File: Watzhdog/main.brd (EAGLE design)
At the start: 100 x 80 mm, 51 parts, among them IC1 C8051F381-GM, IC3 N25Q512A, IC6 MPU-9250, SW2 PTR1TP10R, U1 MCP73831, U2 TPS61200

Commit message: Modified circuit and filename
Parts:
- removed C6: 10uF, rcl:C0402K
- removed R18: (no value), rcl:R0402
- removed R6: 1.2M, rcl:R0402
- removed R7: 220k, rcl:R0402
- removed R8: 2M, rcl:R0402
- removed SJ1: (no value), SparkFun:SJ_3_PASTE2&3
- removed SW2: PTR1TP10R, testpad:TP10R
- added C12: 10uF, CH_passive:1206
- R5: device SparkFun:0603-RES -> rcl:R0402
- U2: value TPS61200 -> TPS61201
- moved C5 335.6 mm to (62.7, 8.51), turned to 180 degrees
- moved C2 329.8 mm to (69.4, 13.9), turned to 90 degrees
- moved JP2 297.5 mm to (47.8, 72.6)
- moved R17 275.6 mm to (22.9, 62.7), turned to 270 degrees
- moved MP 273.4 mm to (21.1, 69.6)
- moved MN 269.9 mm to (23.8, 69.7)
- moved R2 268.6 mm to (71.0, 14.0), turned to 270 degrees
- moved R15 255.5 mm to (24.7, 62.8), turned to 270 degrees
- moved FET1 252.6 mm to (23.7, 66.3)
- moved R14 229.0 mm to (72.6, 38.9), turned to 90 degrees
- moved R9 222.9 mm to (50.7, 72.6), turned to 180 degrees
- moved R13 221.9 mm to (72.6, 36.5), turned to 270 degrees
- moved LED1 219.9 mm to (53.5, 72.6)
- moved R16 215.8 mm to (15.3, 8.42)
- moved S1 213.8 mm to (72.6, 33.5)
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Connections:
- removed net 3.3V: R6.1, SJ1.1
- removed net 5V: R8.1, SJ1.3
- removed net FB: R7.2, SJ1.2, U2.10
- removed net N$12: IC1.32
- removed net N$4: IC1.25, SW2.TP
- net GND: now also C12.2; no longer C6.2, R7.1
- net VBAT: now also C12.1; no longer C6.1
- net VCC: now also U2.10; no longer R6.2, R8.2
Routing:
- net VBAT: track 0.00 -> 16.5 mm
- net GND: track 0.00 -> 15.3 mm, vias 0 -> 3
- net N$11: track 0.00 -> 8.48 mm
- net UVLO: track 0.00 -> 6.35 mm
- net N$6: track 0.00 -> 4.09 mm
- net N$2: track 0.00 -> 2.60 mm
- net N$5: track 0.00 -> 1.59 mm
- net VCC: track 3.05 -> 4.51 mm
- net DGND: track 7.75 -> 8.94 mm

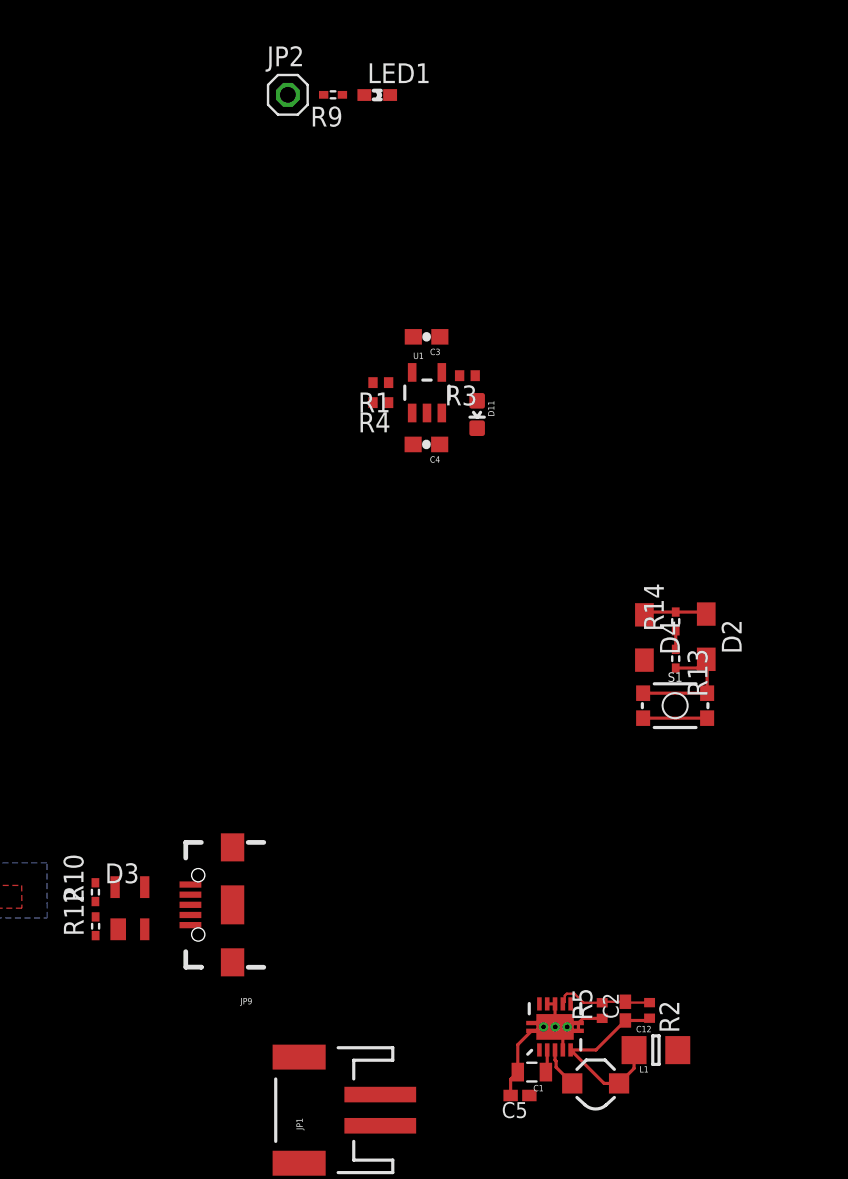
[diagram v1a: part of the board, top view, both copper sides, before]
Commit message: Routed some airwires
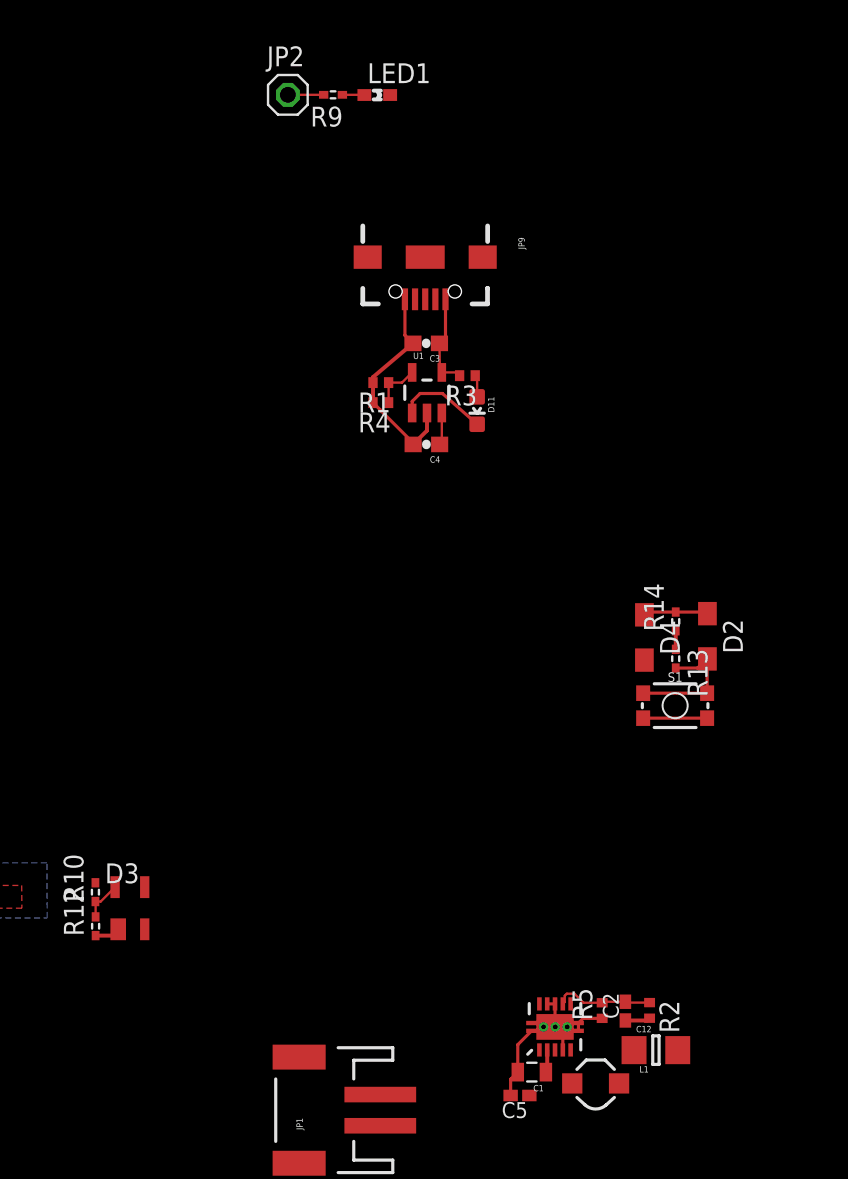
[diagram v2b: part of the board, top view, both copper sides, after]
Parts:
- moved JP9 43.3 mm to (56.6, 62.2), turned to 270 degrees
- moved C3 0.42 mm to (56.7, 56.7)
- moved D11 0.25 mm to (59.9, 52.4)
- moved D2 0.08 mm to (74.7, 37.9)
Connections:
- removed net GND: C1.2, C12.2, C3.2, C4.2, C5.2, JP1.1, JP9.GND1, R1.2, R4.2, R5.1, U1.2, U2.11, U2.12, U2.13, U2.14, U2.15, U2.4, U2.8, U2.9
- net DGND: now also C1.2, C12.2, C3.2, C4.2, C5.2, JP1.1, JP9.GND1, R1.2, R4.2, R5.1, U1.2, U2.11, U2.12, U2.13, U2.14, U2.15, U2.4, U2.8, U2.9
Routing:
- net DGND: track 8.94 -> 40.4 mm, vias 3 -> 6
- net GND: track 15.3 -> 0.00 mm, vias 3 -> 0
- net VBUS: track 0.00 -> 8.78 mm
- net VBAT: track 16.5 -> 7.78 mm
- net STAT: track 0.00 -> 5.86 mm
- net PROG: track 0.00 -> 3.06 mm
- net N$2: track 2.60 -> 0.00 mm
- net N$15: track 0.00 -> 2.30 mm
- net N$9: track 0.00 -> 1.41 mm
- net N$3: track 0.00 -> 1.41 mm

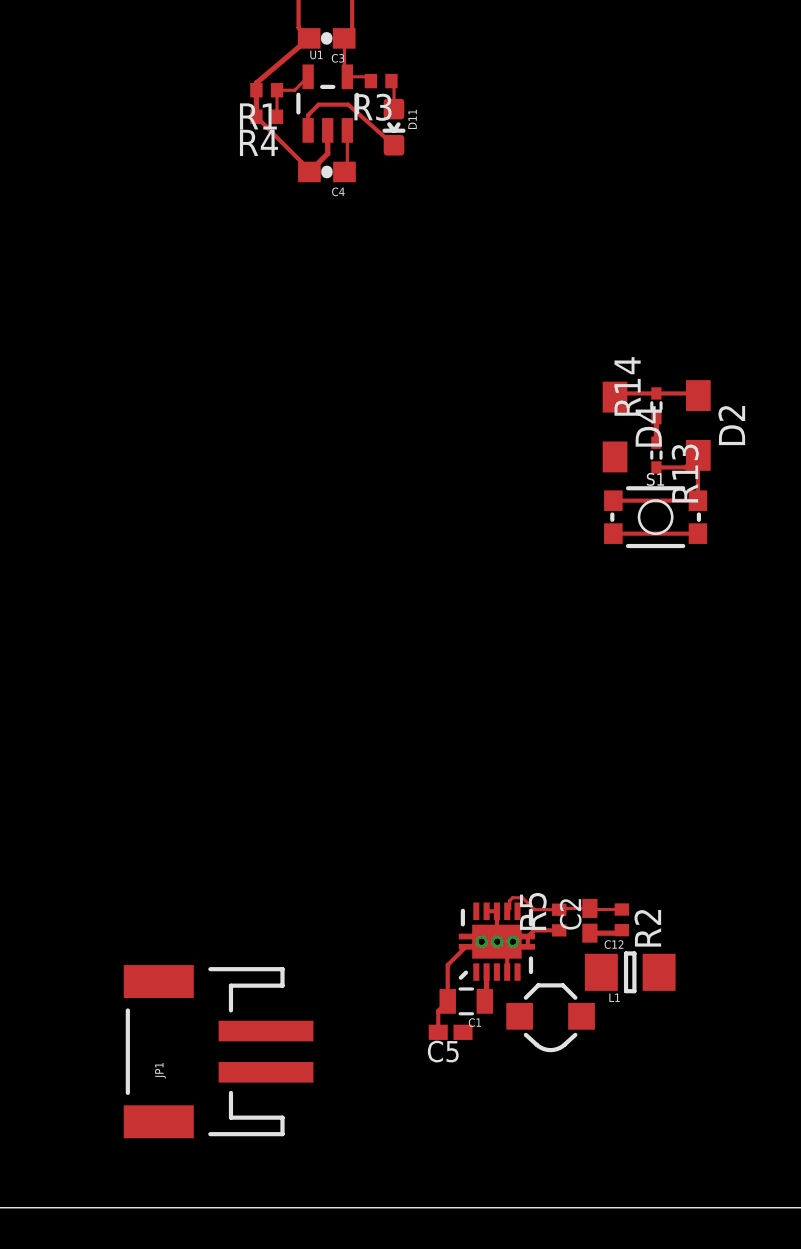
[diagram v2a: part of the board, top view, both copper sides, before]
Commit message: Modified parts' position
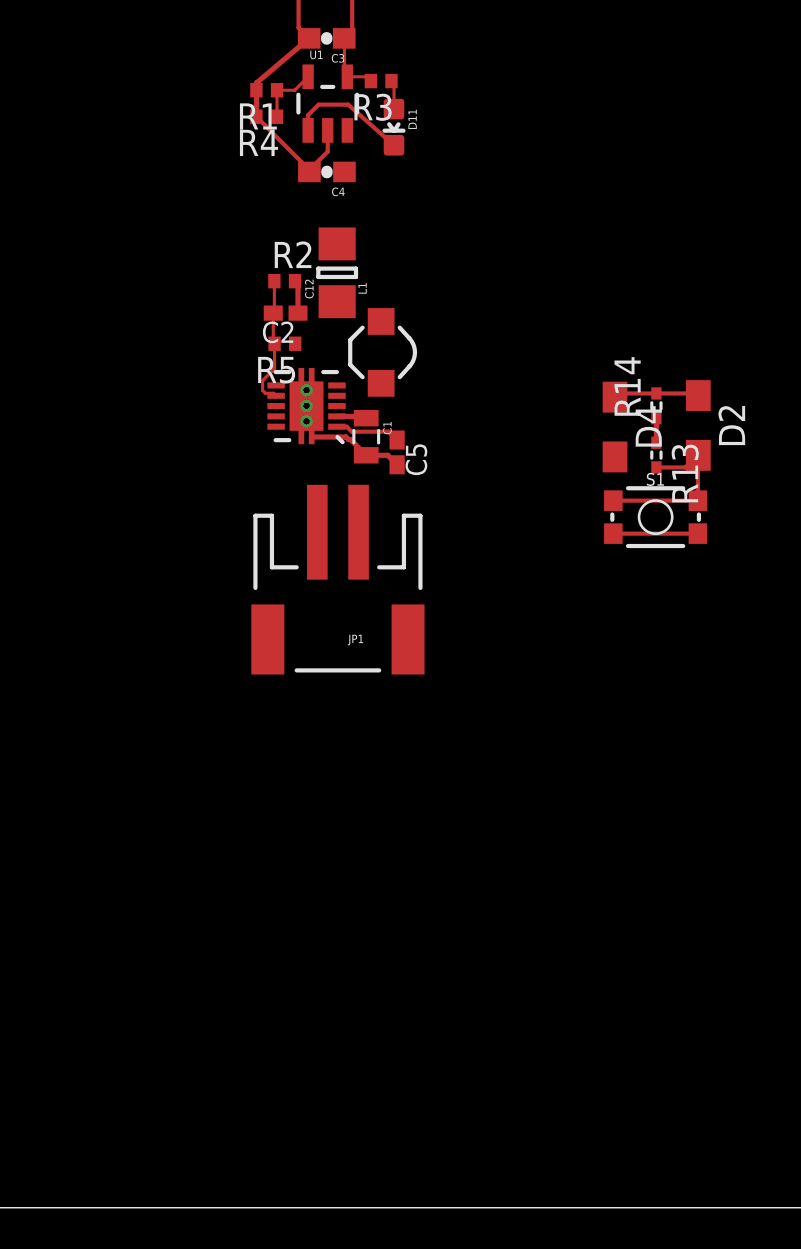
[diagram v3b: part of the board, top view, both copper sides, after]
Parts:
- moved C12 36.8 mm to (57.2, 45.3), turned to 90 degrees
- moved R2 35.0 mm to (54.6, 44.9), turned to 0 degrees
- moved L1 33.2 mm to (59.3, 41.5), turned to 90 degrees
- moved C2 33.0 mm to (54.7, 43.4), turned to 180 degrees
- moved R5 31.0 mm to (54.6, 41.9), turned to 180 degrees
- moved C5 28.2 mm to (60.1, 36.6), turned to 270 degrees
- moved C1 27.8 mm to (58.6, 37.4), turned to 270 degrees
- moved U2 27.6 mm to (55.7, 38.9), turned to 90 degrees
- moved JP1 22.7 mm to (57.2, 29.1), turned to 180 degrees
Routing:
- net DGND: track 40.4 -> 29.4 mm
- net N$1: track 0.00 -> 3.19 mm
- net VBAT: track 7.78 -> 5.71 mm

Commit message: Modified circuit
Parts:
- moved R2 12.4 mm to (64.1, 37.0), turned to 180 degrees
- moved C12 10.8 mm to (57.3, 34.5), turned to 0 degrees
- moved C2 10.6 mm to (64.1, 38.5), turned to 0 degrees
- moved R5 9.67 mm to (64.1, 40.0), turned to 0 degrees
- moved JP1 6.98 mm to (57.2, 22.1)
- moved L1 6.56 mm to (54.1, 37.5), turned to 0 degrees
- moved C5 6.45 mm to (57.5, 42.6), turned to 0 degrees
- moved C1 3.75 mm to (57.3, 40.9), turned to 0 degrees
- moved U2 3.09 mm to (58.6, 38.0), turned to 270 degrees
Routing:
- net UVLO: track 6.35 -> 11.0 mm
- net DGND: track 29.4 -> 24.8 mm
- net VCC: track 4.51 -> 6.90 mm
- net VBAT: track 5.71 -> 4.10 mm
- added copper zone on layer 1, net DGND

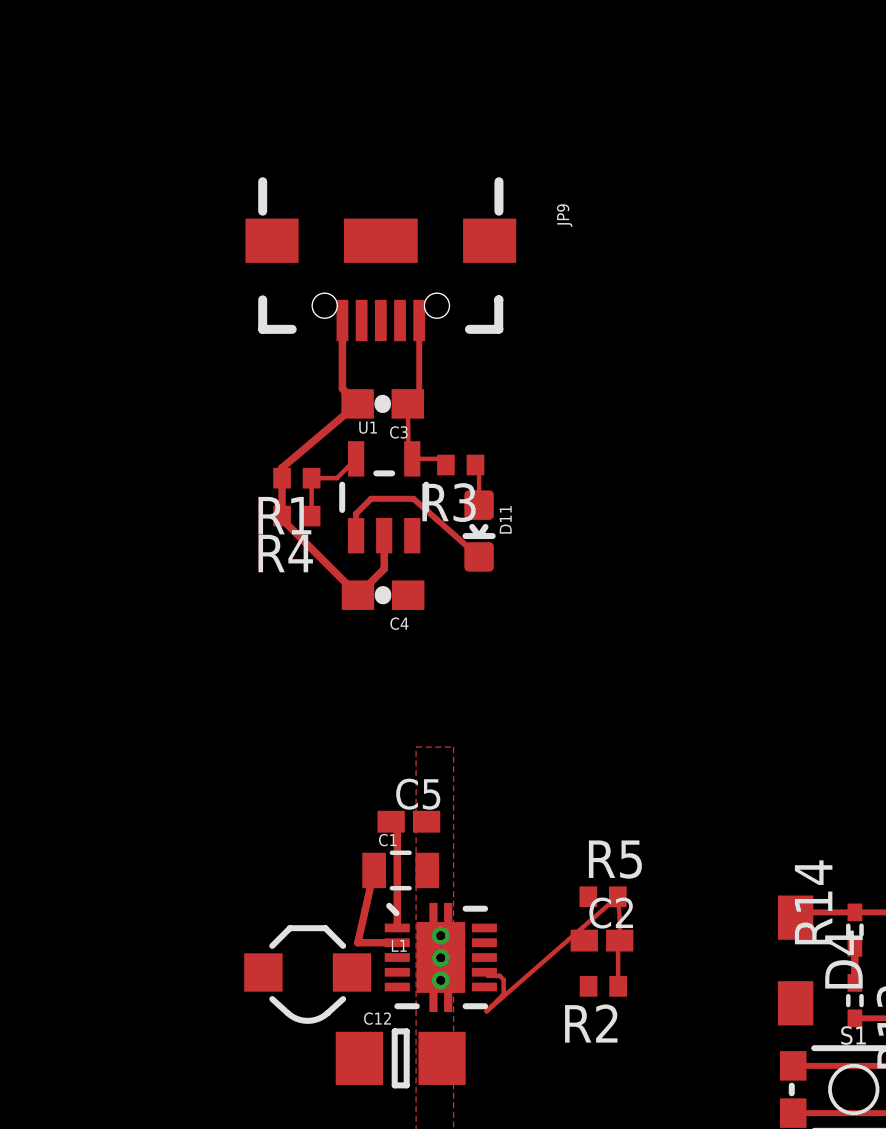
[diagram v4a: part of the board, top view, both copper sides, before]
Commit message: Delete unnecessary resistances
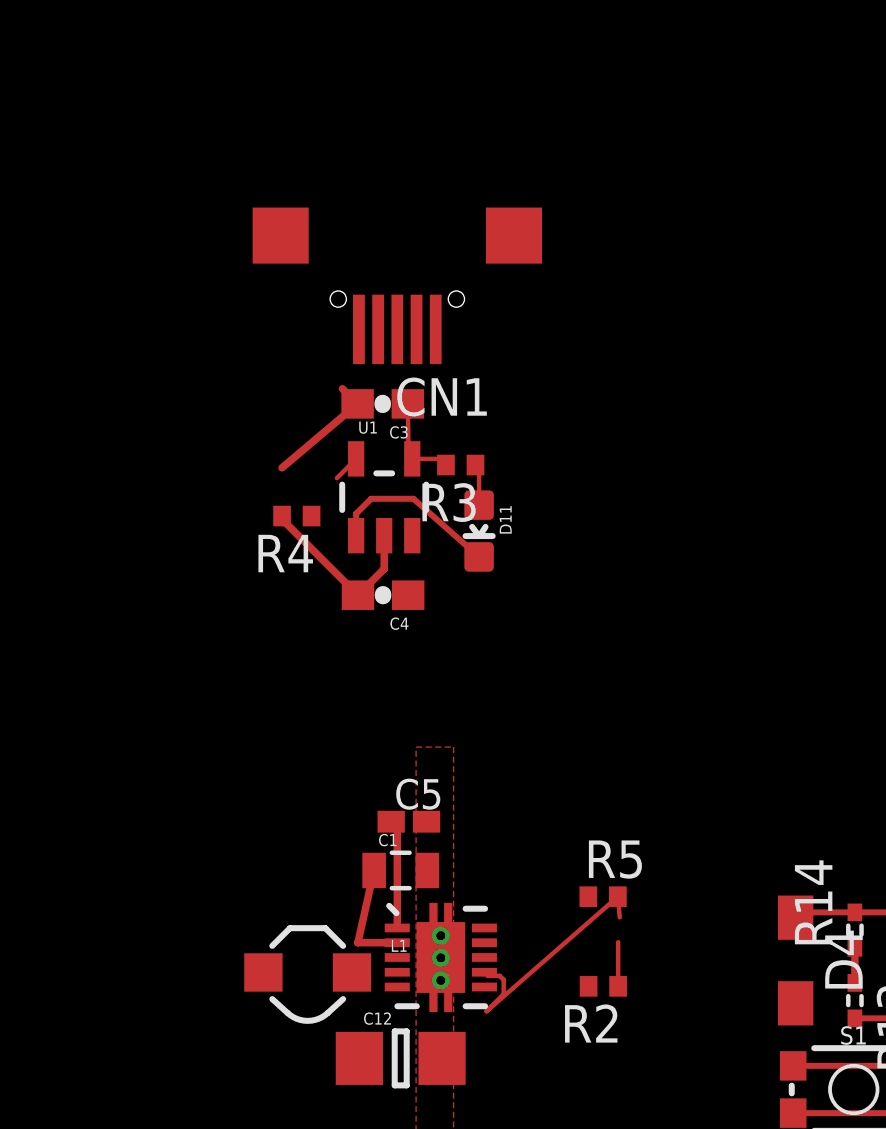
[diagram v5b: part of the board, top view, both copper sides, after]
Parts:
- removed C2: 0.1uF, rcl:C0402K
- removed JP9: Micro USB, SparkFun-Connectors:USB-AB-MICRO-SMD_V03
- removed R1: (no value), rcl:R0402
- added CN1: MICROUSB(MC-5F-02), Connector:MICROUSB(MC-5F-02)
- R4: value 2.0k -> 9.09k
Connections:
- net D+: now also CN1.3; no longer JP9.D+1
- net D-: now also CN1.2; no longer JP9.D-1
- net DGND: now also CN1.5; no longer JP9.GND1, R1.2
- net PROG: no longer R1.1
- net UVLO: no longer C2.2
- net VBAT: no longer C2.1
- net VBUS: now also CN1.1; no longer JP9.VBUS1
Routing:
- net DGND: track 24.8 -> 20.9 mm
- net VBUS: track 8.78 -> 6.32 mm
- net PROG: track 3.06 -> 0.92 mm
- net UVLO: track 11.0 -> 10.2 mm

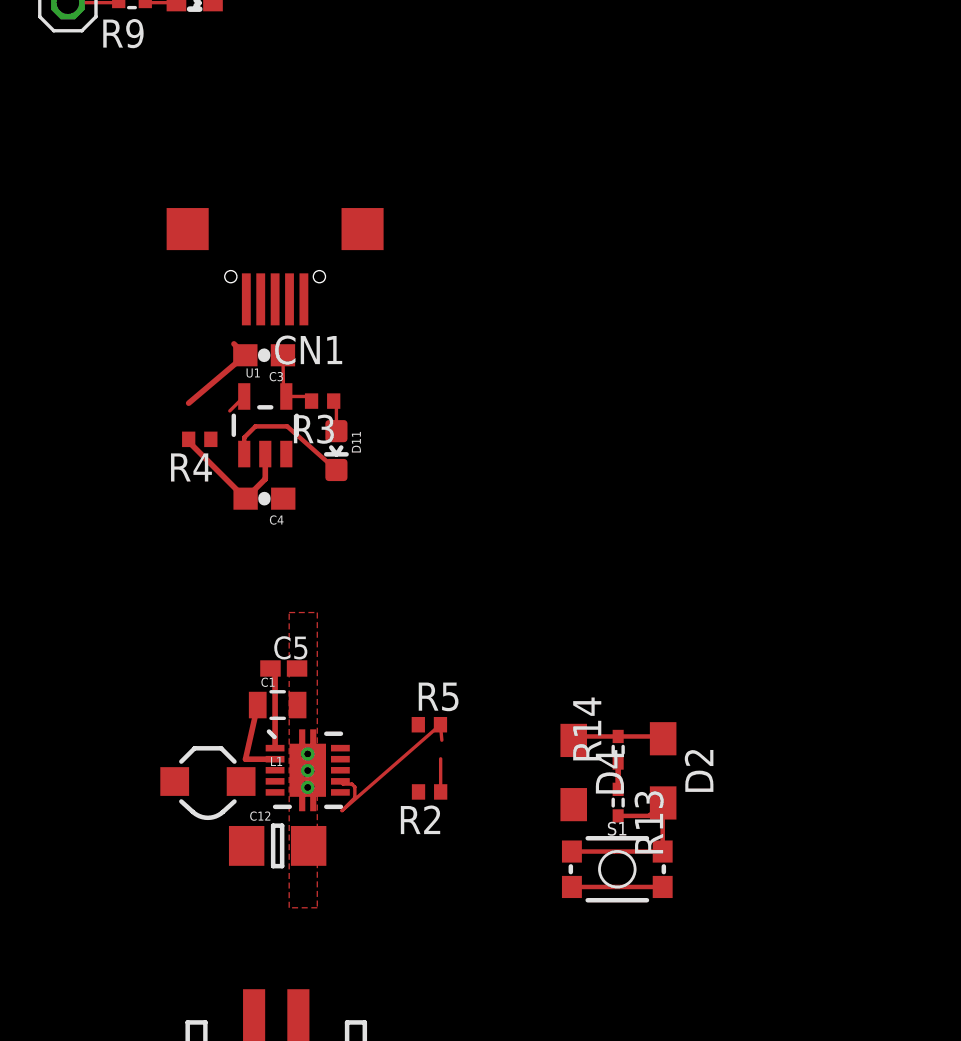
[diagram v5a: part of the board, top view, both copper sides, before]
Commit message: Modified board artwork
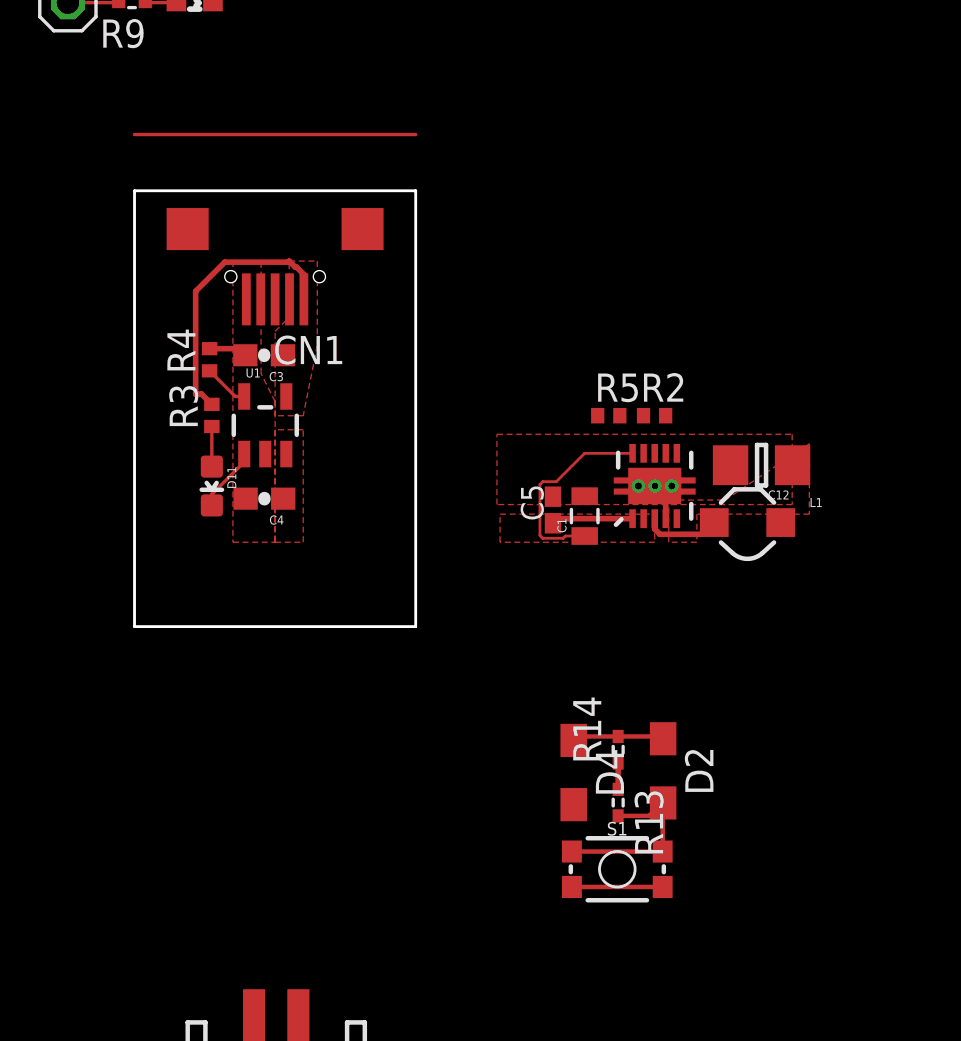
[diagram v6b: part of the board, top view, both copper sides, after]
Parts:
- moved C12 27.8 mm to (79.1, 51.7), turned to 180 degrees
- moved L1 27.0 mm to (78.5, 49.1)
- moved U2 20.3 mm to (74.3, 50.8), turned to 0 degrees
- moved R2 19.8 mm to (74.3, 54.0), turned to 0 degrees
- moved C1 16.3 mm to (71.1, 49.4), turned to 90 degrees
- moved R5 16.1 mm to (72.2, 54.0)
- moved C5 14.1 mm to (69.7, 49.7), turned to 90 degrees
- moved D11 5.85 mm to (54.3, 50.8)
- moved R3 5.05 mm to (54.3, 54.0), turned to 90 degrees
- moved R4 3.62 mm to (54.2, 56.5), turned to 90 degrees
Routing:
- net N$4: track 0.00 -> 12.7 mm
- net UVLO: track 10.2 -> 0.00 mm
- net VBUS: track 6.32 -> 15.8 mm
- net DGND: track 20.9 -> 14.5 mm
- net VCC: track 6.90 -> 12.2 mm
- net N$2: track 0.00 -> 3.48 mm
- net STAT: track 5.86 -> 2.93 mm
- net PROG: track 0.92 -> 2.04 mm
- added copper zone on layer 1, net VBAT
- added copper zone on layer 1, net VBUS
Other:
- outline, holes or cut-outs redrawn
